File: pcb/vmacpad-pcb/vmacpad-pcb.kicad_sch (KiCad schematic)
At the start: 29 parts, among them J1 TYPE-C-31-M12_13, SW1 SW_SPDT, U1 TPD4E05U06DQAR, U2 TXS0101DBVR, U3 STM32F401RCTx, Y1 16MHz

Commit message: Creating the PCB and additional parts
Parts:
- added J2: Conn_01x04_Pin, Connector_PinHeader_2.54mm:PinHeader_1x04_P2.54mm_Vertical, symbol Connector:Conn_01x04_Pin
- added SW2: Alps EM11, Rotary_Encoder:RotaryEncoder_Alps_EC11E-Switch_Vertical_H20mm, symbol Device:RotaryEncoder_Switch
- added SW3: BournsEM14, max_customs:BournsEM14, symbol max_customs:BournsEM14
- added U4: AMS1117-3.3, Package_TO_SOT_SMD:SOT-223-3_TabPin2, symbol Regulator_Linear:AMS1117-3.3
- C1, C10, C2: footprint Capacitor_SMD:C_0805_2012Metric -> Capacitor_SMD:C_1206_3216Metric
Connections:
- net +3.3V: now also J2.1 (Pin_1), U4.2 (VO)
- net GND: now also J2.4 (Pin_4), SW2.C, SW3.4 (VSS), U4.1 (GND)
- net SWCLK: now also J2.3 (Pin_3)
- net SWDIO: now also J2.2 (Pin_2)
- net VCC: now also SW3.3 (VCC), U4.3 (VI)
- net COL0: now reaches U3.20 (PA4)
- net COL1: now reaches U3.21 (PA5)
- net COL2: now reaches U3.22 (PA6)
- net COL3: now reaches U3.23 (PA7)
- net ENC_PADA: now reaches U3.24 (PC4)
- net ENC_PADA: now also SW2.A
- net ENC_PADB: now reaches U3.25 (PC5)
- net ENC_PADB: now also SW2.B
- net ROW0: now reaches U3.26 (PB0)
- net ROW1: now reaches U3.27 (PB1)
- net COL4: now reaches U3.41 (PA8)
- net ROW2: now reaches U3.55 (PB3)
- net ROW3: now reaches U3.56 (PB4)
- new net BOURNS_PADA: SW3.A
- new net BOURNS_PADB: SW3.B
- new net ENC_SW1: SW2.S1, SW3.1
- new net ENC_SW2: SW2.S2, SW3.2
- no-connect marks 2 -> 3
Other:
- note added: "Choose one during soldering! Bourns is in dedicated center!"
- note added: "Encoder"
- note added: "Level Shift Bourns 5V to 3.3V"
- note added: "MIND that switches are footprinted to be mounted on the back! So front := back"
- company: (none) -> 11kbd
- title: (none) -> VMacPad PCB
- moved on the sheet: C1, C2

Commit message: Schematic Rev 1 done
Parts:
- added C17: 10u, Capacitor_SMD:C_0805_2012Metric, symbol Device:C
- added C18, C19: 22n, Capacitor_SMD:C_0805_2012Metric, symbol Device:C
- added J3: Conn_01x04_Pin, Connector_PinHeader_2.54mm:PinHeader_1x04_P2.54mm_Vertical, symbol Connector:Conn_01x04_Pin
- added R5, R6: 1k, Resistor_SMD:R_0805_2012Metric, symbol Device:R_Small
- added R7: 10k, Resistor_SMD:R_0402_1005Metric, symbol Device:R_Small
- C10: footprint Capacitor_SMD:C_1206_3216Metric -> Capacitor_SMD:C_0805_2012Metric
- SW1: value SW_SPDT -> SW_BOOT
- U1: footprint Acheron_Components:USON-10_2.5x1.0mm_P0.5mm -> Package_SON:USON-10_2.5x1.0mm_P0.5mm; LCSC Part # (none) -> C138714; Manufacturer Part # (none) -> TPD4E05U06DQAR
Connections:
- net ENC_PADA is gone; now on net BOURNS_PADA: SW2.A, U3.24 (PC4)
- net ENC_PADB is gone; now on net BOURNS_PADB: SW2.B, U3.25 (PC5)
- net +3.3V: now also J3.1 (Pin_1)
- net BOURNS_PADA: now also C18.1, R5.1
- net BOURNS_PADB: now also C19.1, R6.1
- net GND: now also C17.2, C18.2, C19.2, J3.4 (Pin_4), R7.1
- net VCC: now also C17.1, R5.2, R6.2
- net at U3.28 (PB2): now also R7.2
- net at U3.42 (PA9): now also J3.2 (Pin_2)
- net at U3.43 (PA10): now also J3.3 (Pin_3)
- net DA+ renamed USB+
- net USB+: no longer J1.B7 (D-)
- net DA- renamed USB-
- net USB-: now also J1.B7 (D-)
- no-connect marks 3 -> 32
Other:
- note added: "RC as per datasheet. 5V in acceptable with STM32, see AN"
- note added: "SWDBG"
- note added: "USART1"
- note removed: "Level Shift Bourns 5V to 3.3V"
- moved on the sheet: C1, C2, SW2, SW3, U4

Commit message: Finalizing PCB
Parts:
- C12, C15, C16: footprint Capacitor_SMD:C_0805_2012Metric -> Capacitor_SMD:C_0402_1005Metric
- renumbered D1 to DP1
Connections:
- net BOURNS_PADA: now also U3.8 (PC0); no longer U3.24 (PC4)
- net BOURNS_PADB: now also U3.9 (PC1); no longer U3.25 (PC5)
- net COL4: now also U3.54 (PD2); no longer U3.41 (PA8)
- net ROW0: now also U3.53 (PC12); no longer U3.26 (PB0)
- net ROW1: now also U3.52 (PC11); no longer U3.27 (PB1)
- net ROW2: now also U3.51 (PC10); no longer U3.55 (PB3)
- net ROW3: now also U3.33 (PB12); no longer U3.56 (PB4)
- net USB+: no longer U1.5 (D2-), U1.6 (NC)
- net USB-: now also U1.5 (D2-), U1.6 (NC)
- net VBUS: now also J1.B4 (VBUS)
- no-connect marks 32 -> 31
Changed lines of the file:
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@@
   (junction (at 49.53 56.515) (diameter 0) (color 0 0 0 0)
+  )
+  (junction (at 49.53 27.305) (diameter 0) (color 0 0 0 0)
   )
   (junction (at 200.66 36.83) (diameter 0) (color 0 0 0 0)
@@
   (no_connect (at 297.18 118.11))
   (no_connect (at 264.16 113.03))
-  (no_connect (at 264.16 80.01))
   (no_connect (at 297.18 57.15))
-  (no_connect (at 264.16 72.39))
+  (no_connect (at 301.625 69.85))
   (no_connect (at 297.18 54.61))
   (no_connect (at 297.18 52.07))
   (no_connect (at 297.18 113.03))
+  (no_connect (at 302.26 102.87))
   (no_connect (at 264.16 100.33))
   (no_connect (at 297.18 105.41))
   (no_connect (at 297.18 107.95))
-  (no_connect (at 264.16 105.41))
-  (no_connect (at 297.18 120.65))
   (no_connect (at 49.53 85.725))
   (no_connect (at 297.18 123.19))
-  (no_connect (at 264.16 107.95))
-  (no_connect (at 264.16 77.47))
+  (no_connect (at 264.16 90.17))
+  (no_connect (at 302.26 100.33))
   (no_connect (at 264.16 97.79))
   (no_connect (at 264.16 82.55))
@@
   (no_connect (at 297.18 87.63))
   (no_connect (at 264.16 92.71))
-  (no_connect (at 264.16 102.87))
+  (no_connect (at 302.26 92.71))
   (no_connect (at 297.18 125.73))
   (no_connect (at 297.18 110.49))
   (no_connect (at 49.53 83.185))
+  (no_connect (at 264.16 87.63))
   (no_connect (at 264.16 95.25))
+  (no_connect (at 302.26 95.25))
   (no_connect (at 264.16 110.49))
   (no_connect (at 297.18 115.57))
-  (no_connect (at 49.53 29.845))
   (no_connect (at 297.18 49.53))
   (wire (pts (xy 297.18 82.55) (xy 333.375 82.55))
@@
     (stroke (width 0) (type solid))
   )
+  (wire (pts (xy 260.985 80.01) (xy 264.16 80.01))
+    (stroke (width 0) (type default))
+  )
   (wire (pts (xy 331.47 58.42) (xy 331.47 57.15))
     (stroke (width 0) (type default))
@@
     (stroke (width 0) (type default))
   )
-  (wire (pts (xy 259.715 87.63) (xy 264.16 87.63))
-    (stroke (width 0) (type default))
-  )
   (wire (pts (xy 297.18 95.25) (xy 302.26 95.25))
     (stroke (width 0) (type default))
@@
     (stroke (width 0) (type default))
   )
+  (wire (pts (xy 297.18 120.65) (xy 305.435 120.65))
+    (stroke (width 0) (type default))
+  )
   (wire (pts (xy 233.045 118.11) (xy 234.95 118.11))
     (stroke (width 0) (type solid))
@@
   )
   (wire (pts (xy 174.625 177.165) (xy 177.165 177.165))
-    (stroke (width 0) (type default))
-  )
-  (wire (pts (xy 259.715 90.17) (xy 264.16 90.17))
     (stroke (width 0) (type default))
   )
@@
     (stroke (width 0) (type default))
   )
+  (wire (pts (xy 260.35 72.39) (xy 264.16 72.39))
+    (stroke (width 0) (type default))
+  )
   (wire (pts (xy 333.375 66.04) (xy 332.105 66.04))
     (stroke (width 0) (type default))
@@
     (stroke (width 0) (type default))
   )
+  (wire (pts (xy 49.53 27.305) (xy 49.53 29.845))
+    (stroke (width 0) (type default))
+  )
   (wire (pts (xy 187.96 36.83) (xy 200.66 36.83))
     (stroke (width 0) (type default))
@@
     (stroke (width 0) (type solid))
   )
+  (wire (pts (xy 259.715 102.87) (xy 264.16 102.87))
+    (stroke (width 0) (type default))
+  )
   (wire (pts (xy 109.855 46.99) (xy 109.855 49.53))
     (stroke (width 0) (type default))
@@
   )
   (wire (pts (xy 139.065 172.72) (xy 133.985 172.72))
+    (stroke (width 0) (type default))
+  )
+  (wire (pts (xy 259.715 105.41) (xy 264.16 105.41))
+    (stroke (width 0) (type default))
+  )
+  (wire (pts (xy 260.985 77.47) (xy 264.16 77.47))
     (stroke (width 0) (type default))
   )
@@
   )
   (wire (pts (xy 297.18 92.71) (xy 302.26 92.71))
+    (stroke (width 0) (type default))
+  )
+  (wire (pts (xy 259.715 107.95) (xy 264.16 107.95))
     (stroke (width 0) (type default))
   )
@@
     (effects (font (size 0.508 0.508)) (justify left bottom))
   )
-  (global_label "ROW1" (shape input) (at 302.26 95.25 0) (fields_autoplaced)
-    (effects (font (size 1.27 1.27)) (justify left))
-    (property "Intersheetrefs" "${INTERSHEET_REFS}" (at 310.5066 95.25 0)
-      (effects (font (size 1.27 1.27)) (justify left) hide)
+  (global_label "ROW1" (shape input) (at 259.715 105.41 180) (fields_autoplaced)
+    (effects (font (size 1.27 1.27)) (justify right))
+    (property "Intersheetrefs" "${INTERSHEET_REFS}" (at 251.4684 105.41 0)
+      (effects (font (size 1.27 1.27)) (justify right) hide)
     )
   )
@@
     )
   )
-  (global_label "COL4" (shape input) (at 301.625 69.85 0) (fields_autoplaced)
-    (effects (font (size 1.27 1.27)) (justify left))
-    (property "Intersheetrefs" "${INTERSHEET_REFS}" (at 309.4483 69.85 0)
-      (effects (font (size 1.27 1.27)) (justify left) hide)
+  (global_label "COL4" (shape input) (at 260.35 72.39 180) (fields_autoplaced)
+    (effects (font (size 1.27 1.27)) (justify right))
+    (property "Intersheetrefs" "${INTERSHEET_REFS}" (at 252.5267 72.39 0)
+      (effects (font (size 1.27 1.27)) (justify right) hide)
     )
   )
@@
     )
   )
-  (global_label "ENC_PADB" (shape input) (at 259.715 90.17 180) (fields_autoplaced)
+  (global_label "ENC_PADB" (shape input) (at 260.985 80.01 180) (fields_autoplaced)
     (effects (font (size 1.27 1.27)) (justify right))
-    (property "Intersheetrefs" "${INTERSHEET_REFS}" (at 247.1141 90.17 0)
+    (property "Intersheetrefs" "${INTERSHEET_REFS}" (at 248.3841 80.01 0)
       (effects (font (size 1.27 1.27)) (justify right) hide)
     )
@@
     )
   )
-  (global_label "ENC_PADA" (shape input) (at 259.715 87.63 180) (fields_autoplaced)
+  (global_label "ENC_PADA" (shape input) (at 260.985 77.47 180) (fields_autoplaced)
     (effects (font (size 1.27 1.27)) (justify right))
-    (property "Intersheetrefs" "${INTERSHEET_REFS}" (at 247.2955 87.63 0)
+    (property "Intersheetrefs" "${INTERSHEET_REFS}" (at 248.5655 77.47 0)
       (effects (font (size 1.27 1.27)) (justify right) hide)
     )
@@
     )
   )
+  (global_label "USB-" (shape output) (at 111.125 52.07 0)
+    (effects (font (size 1.27 1.27)) (justify left))
+    (property "Intersheetrefs" "${INTERSHEET_REFS}" (at 111.125 52.07 0)
+      (effects (font (size 1.27 1.27)) hide)
+    )
+  )
   (global_label "OSC_IN" (shape input) (at 262.255 64.77 180) (fields_autoplaced)
     (effects (font (size 1.27 1.27)) (justify right))
@@
     )
   )
-  (global_label "ROW0" (shape input) (at 302.26 92.71 0) (fields_autoplaced)
-    (effects (font (size 1.27 1.27)) (justify left))
-    (property "Intersheetrefs" "${INTERSHEET_REFS}" (at 310.5066 92.71 0)
-      (effects (font (size 1.27 1.27)) (justify left) hide)
+  (global_label "ROW0" (shape input) (at 259.715 107.95 180) (fields_autoplaced)
+    (effects (font (size 1.27 1.27)) (justify right))
+    (property "Intersheetrefs" "${INTERSHEET_REFS}" (at 251.4684 107.95 0)
+      (effects (font (size 1.27 1.27)) (justify right) hide)
     )
   )
@@
     )
   )
-  (global_label "ROW3" (shape input) (at 302.26 102.87 0) (fields_autoplaced)
+  (global_label "ROW3" (shape input) (at 305.435 120.65 0) (fields_autoplaced)
     (effects (font (size 1.27 1.27)) (justify left))
-    (property "Intersheetrefs" "${INTERSHEET_REFS}" (at 310.5066 102.87 0)
+    (property "Intersheetrefs" "${INTERSHEET_REFS}" (at 313.6816 120.65 0)
       (effects (font (size 1.27 1.27)) (justify left) hide)
     )
   )
-  (global_label "ROW2" (shape input) (at 302.26 100.33 0) (fields_autoplaced)
-    (effects (font (size 1.27 1.27)) (justify left))
-    (property "Intersheetrefs" "${INTERSHEET_REFS}" (at 310.5066 100.33 0)
-      (effects (font (size 1.27 1.27)) (justify left) hide)
+  (global_label "ROW2" (shape input) (at 259.715 102.87 180) (fields_autoplaced)
+    (effects (font (size 1.27 1.27)) (justify right))
+    (property "Intersheetrefs" "${INTERSHEET_REFS}" (at 251.4684 102.87 0)
+      (effects (font (size 1.27 1.27)) (justify right) hide)
     )
   )
@@
     (property "Intersheetrefs" "${INTERSHEET_REFS}" (at 140.2526 182.245 0)
       (effects (font (size 1.27 1.27)) (justify right) hide)
-    )
-  )
-  (global_label "USB+" (shape output) (at 111.125 52.07 0)
-    (effects (font (size 1.27 1.27)) (justify left))
-    (property "Intersheetrefs" "${INTERSHEET_REFS}" (at 111.125 52.07 0)
-      (effects (font (size 1.27 1.27)) hide)
     )
   )
@@
       (effects (font (size 1.27 1.27)) (justify left))
     )
-    (property "Footprint" "Capacitor_SMD:C_0805_2012Metric" (at 220.0402 57.785 0)
+    (property "Footprint" "Capacitor_SMD:C_0402_1005Metric" (at 220.0402 57.785 0)
       (effects (font (size 1.27 1.27)) hide)
     )
@@
       (effects (font (size 1.27 1.27)) (justify left))
     )
-    (property "Footprint" "Capacitor_SMD:C_0805_2012Metric" (at 56.2102 213.36 0)
+    (property "Footprint" "Capacitor_SMD:C_0402_1005Metric" (at 56.2102 213.36 0)
       (effects (font (size 1.27 1.27)) hide)
     )
@@
   (symbol (lib_id "Device:D_TVS") (at 92.71 90.17 270) (mirror x) (unit 1)
     (in_bom yes) (on_board yes) (dnp no)
-    (property "Reference" "D1" (at 88.9 90.17 0)
+    (property "Reference" "DP1" (at 88.9 90.17 0)
       (effects (font (size 0.762 0.762)))
     )
@@
       (project "vmacpad-pcb"
         (path "/b8c85975-4701-4a7a-8c2b-ed47ce17715e"
-          (reference "D1") (unit 1)
+          (reference "DP1") (unit 1)
         )
       )
@@
       (effects (font (size 1.27 1.27)) (justify left))
     )
-    (property "Footprint" "Capacitor_SMD:C_0805_2012Metric" (at 69.5452 213.36 0)
-      (effects (font (size 1.27 1.27)) hide)
-    )
+    (property "Footprint" "Capacitor_SMD:C_0402_1005Metric" (at 69.5452 213.36 0)
+      (effects (font (size 1.27 1.27)) hide)
+    )

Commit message: Fix properties
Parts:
- C1, C2: Package C0805 -> C1206
- C10, C17, C18, C19: Package (none) -> C0805
- C12, C15, C16, C5, C6, C7, C8, C9: Package (none) -> C0402
- J2: Package (none) -> 2.54 4x2
- J3: Package (none) -> 2.54 4x1
- R1, R2: Package R0603 -> R0805
- R4: Package (none) -> R0805
- R7: Package R0805 -> R0402
- U1: LCSC Part # C138714 -> (none)
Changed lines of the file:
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@@
+      (effects (font (size 1.27 1.27)) hide)
+    )
+    (property "Package" "C0805" (at 187.96 40.64 0)
       (effects (font (size 1.27 1.27)) hide)
     )
@@
       (effects (font (size 1.27 1.27)) hide)
     )
-    (property "Package" "R0603" (at 53.34 40.005 90)
+    (property "Package" "R0805" (at 53.34 40.005 90)
       (effects (font (size 1.27 1.27)) hide)
     )
@@
       (effects (font (size 1.27 1.27)) hide)
     )
-    (property "Package" "R0805" (at 313.69 97.79 0)
+    (property "Package" "R0402" (at 313.69 97.79 0)
       (effects (font (size 1.27 1.27)) hide)
     )
@@
   (symbol (lib_id "Device:R") (at 222.25 70.485 90) (unit 1)
     (in_bom yes) (on_board yes) (dnp no)
-    (property "Reference" "R4" (at 222.25 66.675 90)
+    (property "Reference" "R4" (at 222.25 68.58 90)
       (effects (font (size 1.27 1.27)))
     )
-    (property "Value" "10k" (at 222.25 68.58 90)
+    (property "Value" "10k" (at 222.25 70.485 90)
       (effects (font (size 1.27 1.27)))
     )
@@
     )
     (property "Datasheet" "~" (at 222.25 70.485 0)
+      (effects (font (size 1.27 1.27)) hide)
+    )
+    (property "Package" "R0805" (at 222.25 70.485 90)
       (effects (font (size 1.27 1.27)) hide)
     )
@@
       (effects (font (size 1.27 1.27)) hide)
     )
-    (property "Package" "C0805" (at 92.71 158.75 0)
+    (property "Package" "C1206" (at 92.71 158.75 0)
       (effects (font (size 1.27 1.27)) hide)
     )
@@
       (effects (font (size 1.27 1.27)) hide)
     )
+    (property "Package" "C0805" (at 151.13 217.805 0)
+      (effects (font (size 1.27 1.27)) hide)
+    )
     (pin "1")
     (pin "2")
@@
     )
     (property "Datasheet" "~" (at 338.455 82.55 0)
+      (effects (font (size 1.27 1.27)) hide)
+    )
+    (property "Package" "2.54 4x2" (at 338.455 82.55 0)
       (effects (font (size 1.27 1.27)) hide)
     )
@@
       (effects (font (size 1.27 1.27)) hide)
     )
+    (property "Package" "2.54 4x1" (at 338.455 60.96 0)
+      (effects (font (size 1.27 1.27)) hide)
+    )
     (pin "1")
     (pin "2")
@@
       (effects (font (size 1.27 1.27)) hide)
     )
+    (property "Package" "C0402" (at 219.075 53.975 0)
+      (effects (font (size 1.27 1.27)) hide)
+    )
     (pin "1")
     (pin "2")
@@
       (effects (font (size 1.27 1.27)) hide)
     )
+    (property "Package" "C0402" (at 238.76 40.64 0)
+      (effects (font (size 1.27 1.27)) hide)
+    )
     (pin "1")
     (pin "2")
@@
       (effects (font (size 1.27 1.27)) hide)
     )
-    (property "Package" "C0805" (at 57.15 158.75 0)
+    (property "Package" "C1206" (at 57.15 158.75 0)
       (effects (font (size 1.27 1.27)) hide)
     )
@@
       (effects (font (size 1.27 1.27)) hide)
     )
+    (property "Package" "C0402" (at 55.245 209.55 0)
+      (effects (font (size 1.27 1.27)) hide)
+    )
     (pin "1")
     (pin "2")
@@
       (effects (font (size 1.27 1.27)) hide)
     )
+    (property "Package" "C0402" (at 251.46 40.64 0)
+      (effects (font (size 1.27 1.27)) hide)
+    )
     (pin "1")
     (pin "2")
@@
       (effects (font (size 1.27 1.27)) hide)
     )
+    (property "Package" "C0402" (at 200.66 40.64 0)
+      (effects (font (size 1.27 1.27)) hide)
+    )
     (pin "1")
     (pin "2")
@@
       (effects (font (size 1.27 1.27)) hide)
     )
+    (property "Package" "C0402" (at 213.36 40.64 0)
+      (effects (font (size 1.27 1.27)) hide)
+    )
     (pin "1")
     (pin "2")
@@
     )
     (property "Datasheet" "~" (at 180.34 179.07 0)
+      (effects (font (size 1.27 1.27)) hide)
+    )
+    (property "Package" "C0805" (at 180.34 179.07 0)
       (effects (font (size 1.27 1.27)) hide)
     )
@@
       (effects (font (size 1.27 1.27)) hide)
     )
-    (property "Package" "R0603" (at 53.34 45.085 90)
+    (property "Package" "R0805" (at 53.34 45.085 90)
       (effects (font (size 1.27 1.27)) hide)
     )
@@
       (effects (font (size 1.27 1.27)) hide)
     )
+    (property "Package" "C0402" (at 68.58 209.55 0)
+      (effects (font (size 1.27 1.27)) hide)
+    )
     (pin "1")
     (pin "2")
@@
     )
     (property "Datasheet" "~" (at 156.845 208.915 0)
+      (effects (font (size 1.27 1.27)) hide)
+    )
+    (property "Package" "C0805" (at 156.845 208.915 0)
       (effects (font (size 1.27 1.27)) hide)
     )
@@
     )
     (property "Manufacturer Part #" "TPD4E05U06DQAR" (at 97.155 27.94 0)
-      (effects (font (size 1.27 1.27)) hide)
-    )
-    (property "LCSC Part #" "C138714" (at 97.155 25.4 0)
       (effects (font (size 1.27 1.27)) hide)
     )
@@
       (effects (font (size 1.27 1.27)) hide)
     )
+    (property "Package" "C0402" (at 226.06 40.64 0)
+      (effects (font (size 1.27 1.27)) hide)
+    )

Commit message: Fixes to part numbers and production
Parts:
- C1, C2: LCSC (none) -> C2858005; LCSC Part No (none) -> C2858005
- C10, C17: LCSC (none) -> C88484; LCSC Part No (none) -> C88484
- C11, C13: LCSC (none) -> C368809; LCSC Part No (none) -> C368809
- C12, C5, C6, C7, C8, C9: LCSC (none) -> C77020; LCSC Part No (none) -> C77020
- C14: LCSC (none) -> C60133; LCSC Part No (none) -> C60133
- C15, C16: LCSC (none) -> C115606; LCSC Part No (none) -> C115606
- C18, C19: LCSC (none) -> C51574; LCSC Part No (none) -> C51574
- C3, C4: footprint Capacitor_SMD:C_0805_2012Metric -> Capacitor_SMD:C_0402_1005Metric; LCSC (none) -> C77020; LCSC Part No (none) -> C77020; Package C0805 -> C0402
- DP1: LCSC (none) -> C123799
- F1: LCSC (none) -> C883134; LCSC Part No C135342 -> C883134
- J1: LCSC (none) -> C165948
- J2, J3: now left out of the parts list
- L1: LCSC (none) -> C33600
- R1, R2: LCSC (none) -> C144526; LCSC Part No (none) -> C144526
- R3, R4: LCSC (none) -> C84376; LCSC Part No (none) -> C84376
- R5, R6: LCSC (none) -> C115316; LCSC Part No (none) -> C115316
- R7: LCSC (none) -> C60490; LCSC Part No (none) -> C60490
- SW1: LCSC (none) -> C431540
- U1: LCSC (none) -> C138714
- U2: LCSC (none) -> C132604
- U3: LCSC (none) -> C74524
- U4: LCSC (none) -> C6186
- Y1: LCSC (none) -> C112972

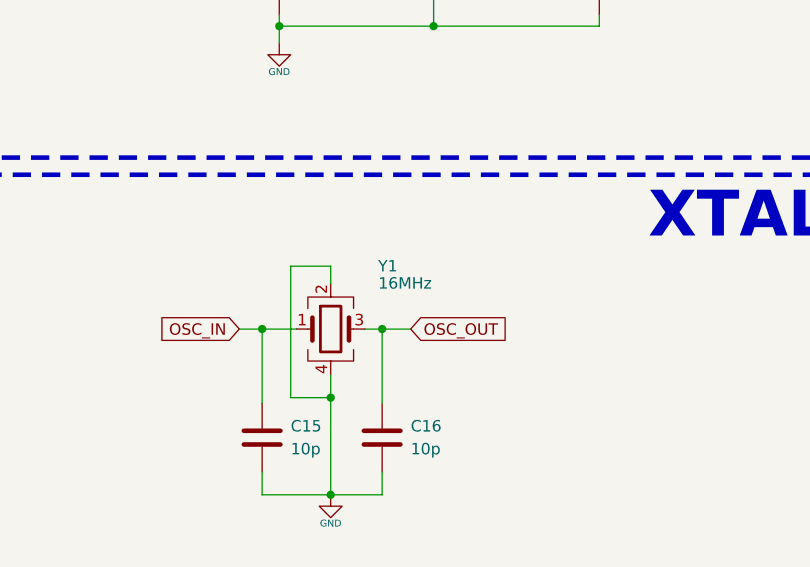
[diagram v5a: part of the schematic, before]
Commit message: Change HSE to 8MHz
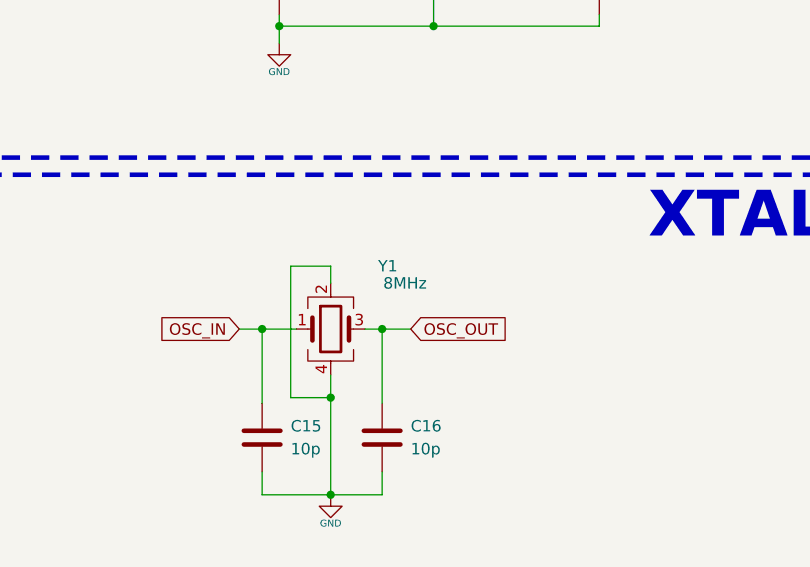
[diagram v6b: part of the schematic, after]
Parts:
- Y1: value 16MHz -> 8MHz; LCSC C112972 -> C400090; LCSC Part No C112972 -> C400090
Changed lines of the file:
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@@
       (effects (font (size 1.27 1.27)))
     )
-    (property "Value" "16MHz" (at 71.12 192.405 0)
+    (property "Value" "8MHz" (at 71.12 192.405 0)
       (effects (font (size 1.27 1.27)))
     )
@@
       (effects (font (size 1.27 1.27)) hide)
     )
-    (property "LCSC Part No" "C112972" (at 62.865 197.485 0)
+    (property "LCSC Part No" "C400090" (at 62.865 197.485 0)
       (effects (font (size 1.27 1.27)) hide)
     )
-    (property "LCSC" "C112972" (at 62.865 197.485 0)
+    (property "LCSC" "C400090" (at 62.865 197.485 0)
       (effects (font (size 1.27 1.27)) hide)
     )
